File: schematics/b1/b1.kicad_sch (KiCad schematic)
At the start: 0 parts

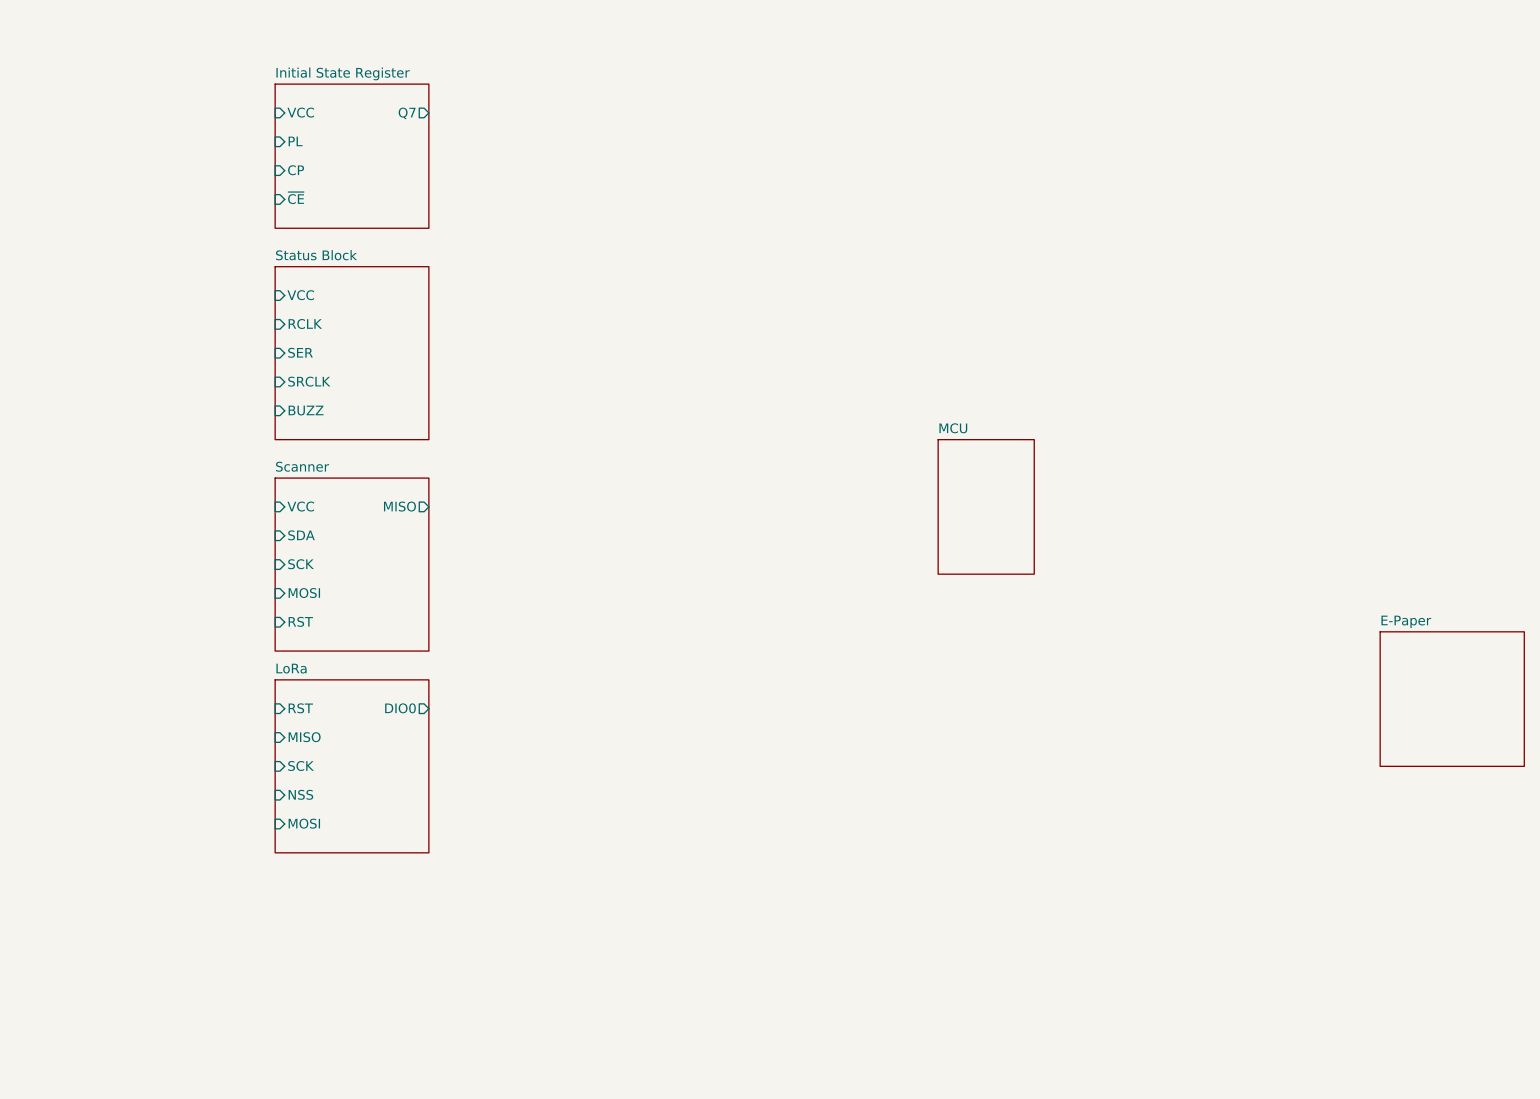
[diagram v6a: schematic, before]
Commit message: Added schematic page for e-paper block.
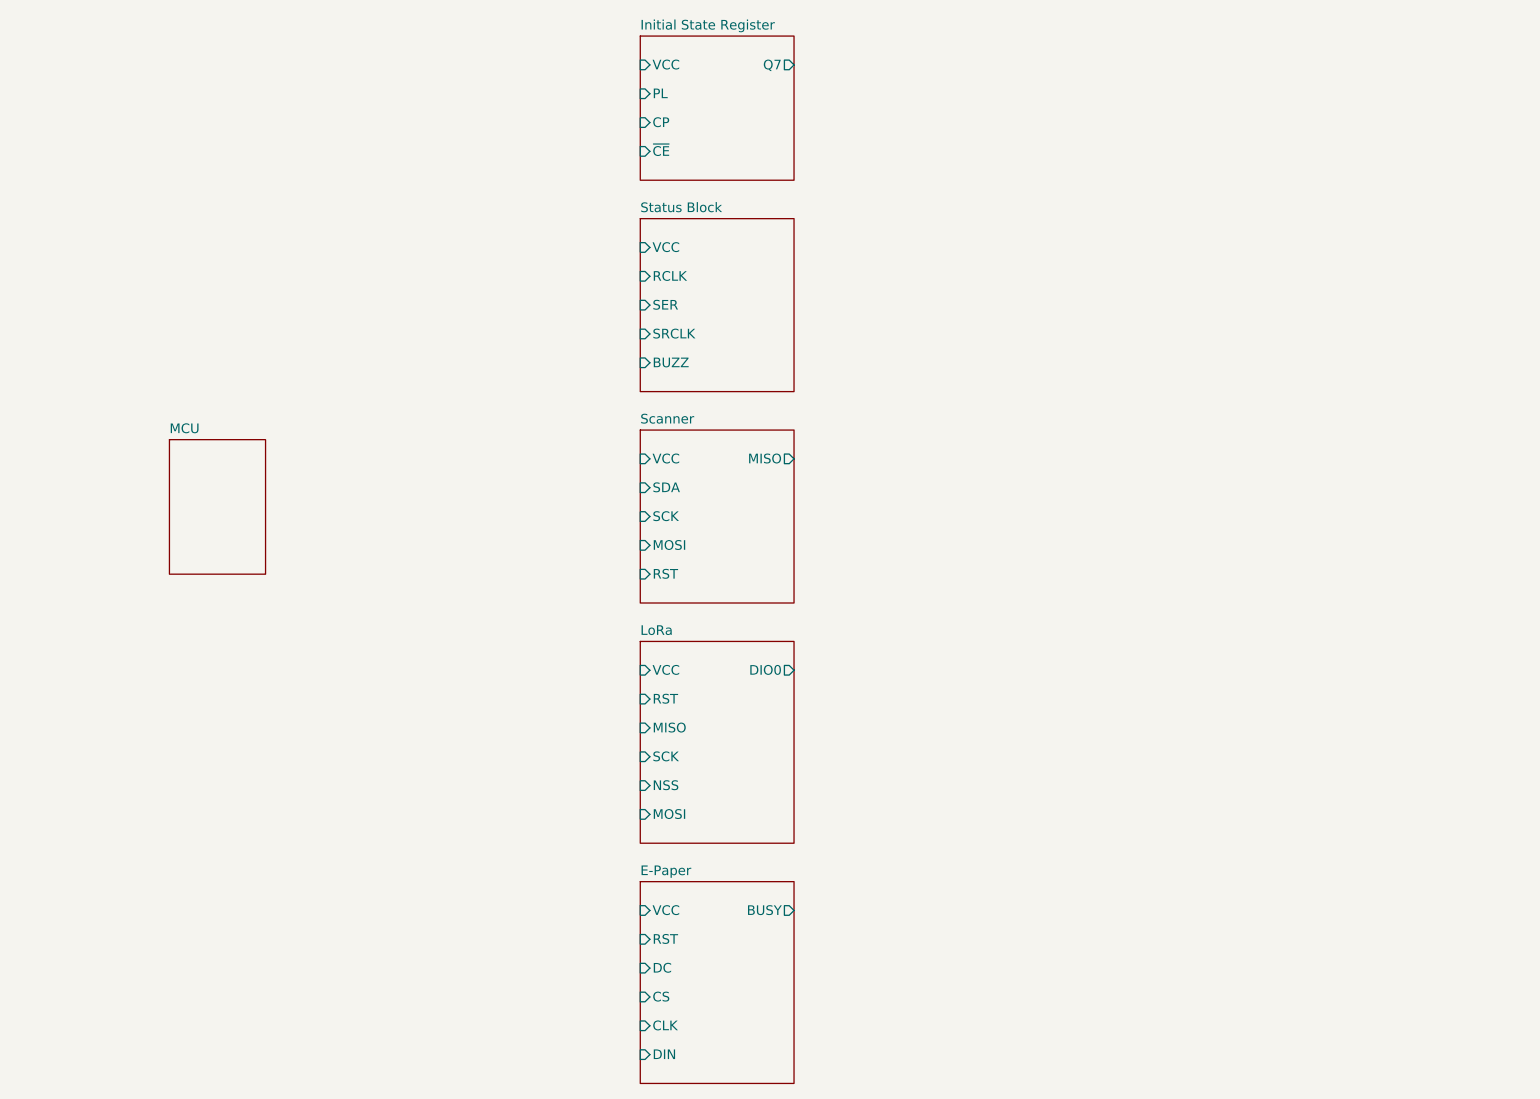
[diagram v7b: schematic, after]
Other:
- sheet E-Paper ports: added BUSY, CLK, CS, DC, DIN, RST, VCC; removed none
- sheet LoRa ports: added VCC; removed none
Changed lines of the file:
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@@
     (comment 4 "A B1 (Badger One) node is the core hardware unit of the Badger sytem. It handles card")
   )
-  (sheet (at 78.74 29.21) (size 20.32 19.05) (fields_autoplaced)
+  (sheet (at 127 22.86) (size 20.32 19.05) (fields_autoplaced)
     (stroke (width 0.1524) (type solid))
     (fill (color 0 0 0 0.0000))
-    (property "Sheetname" "Initial State Register" (at 78.74 28.4984 0)
+    (property "Sheetname" "Initial State Register" (at 127 22.1484 0)
       (effects (font (size 1.27 1.27)) (justify left bottom))
     )
-    (property "Sheetfile" "initial_state_register.kicad_sch" (at 78.74 48.8446 0)
+    (property "Sheetfile" "initial_state_register.kicad_sch" (at 127 42.4946 0)
       (effects (font (size 1.27 1.27)) (justify left top) hide)
     )
-    (pin "PL" input (at 78.74 36.83 180)
+    (pin "PL" input (at 127 30.48 180)
       (effects (font (size 1.27 1.27)) (justify left))
     )
-    (pin "CP" input (at 78.74 40.64 180)
+    (pin "CP" input (at 127 34.29 180)
       (effects (font (size 1.27 1.27)) (justify left))
     )
-    (pin "~{CE}" input (at 78.74 44.45 180)
+    (pin "~{CE}" input (at 127 38.1 180)
       (effects (font (size 1.27 1.27)) (justify left))
     )
-    (pin "Q7" output (at 99.06 33.02 0)
+    (pin "Q7" output (at 147.32 26.67 0)
       (effects (font (size 1.27 1.27)) (justify right))
     )
-    (pin "VCC" input (at 78.74 33.02 180)
+    (pin "VCC" input (at 127 26.67 180)
       (effects (font (size 1.27 1.27)) (justify left))
     )
@@
     )
   )
-  (sheet (at 78.74 81.28) (size 20.32 22.86) (fields_autoplaced)
+  (sheet (at 127 74.93) (size 20.32 22.86) (fields_autoplaced)
     (stroke (width 0.1524) (type solid))
     (fill (color 0 0 0 0.0000))
-    (property "Sheetname" "Scanner" (at 78.74 80.5684 0)
+    (property "Sheetname" "Scanner" (at 127 74.2184 0)
       (effects (font (size 1.27 1.27)) (justify left bottom))
     )
-    (property "Sheetfile" "scanner.kicad_sch" (at 78.74 104.7246 0)
+    (property "Sheetfile" "scanner.kicad_sch" (at 127 98.3746 0)
       (effects (font (size 1.27 1.27)) (justify left top) hide)
     )
-    (pin "MISO" output (at 99.06 85.09 0)
+    (pin "MISO" output (at 147.32 78.74 0)
       (effects (font (size 1.27 1.27)) (justify right))
     )
-    (pin "VCC" input (at 78.74 85.09 180)
+    (pin "VCC" input (at 127 78.74 180)
       (effects (font (size 1.27 1.27)) (justify left))
     )
-    (pin "SDA" input (at 78.74 88.9 180)
+    (pin "SDA" input (at 127 82.55 180)
       (effects (font (size 1.27 1.27)) (justify left))
     )
-    (pin "SCK" input (at 78.74 92.71 180)
+    (pin "SCK" input (at 127 86.36 180)
       (effects (font (size 1.27 1.27)) (justify left))
     )
-    (pin "MOSI" input (at 78.74 96.52 180)
+    (pin "MOSI" input (at 127 90.17 180)
       (effects (font (size 1.27 1.27)) (justify left))
     )
-    (pin "RST" input (at 78.74 100.33 180)
+    (pin "RST" input (at 127 93.98 180)
       (effects (font (size 1.27 1.27)) (justify left))
     )
@@
     )
   )
-  (sheet (at 224.79 101.6) (size 19.05 17.78) (fields_autoplaced)
+  (sheet (at 127 134.62) (size 20.32 26.67) (fields_autoplaced)
     (stroke (width 0.1524) (type solid))
     (fill (color 0 0 0 0.0000))
-    (property "Sheetname" "E-Paper" (at 224.79 100.8884 0)
+    (property "Sheetname" "E-Paper" (at 127 133.9084 0)
       (effects (font (size 1.27 1.27)) (justify left bottom))
     )
-    (property "Sheetfile" "epaper.kicad_sch" (at 224.79 119.9646 0)
+    (property "Sheetfile" "epaper.kicad_sch" (at 127 161.8746 0)
       (effects (font (size 1.27 1.27)) (justify left top) hide)
+    )
+    (pin "BUSY" output (at 147.32 138.43 0)
+      (effects (font (size 1.27 1.27)) (justify right))
+    )
+    (pin "RST" input (at 127 142.24 180)
+      (effects (font (size 1.27 1.27)) (justify left))
+    )
+    (pin "DC" input (at 127 146.05 180)
+      (effects (font (size 1.27 1.27)) (justify left))
+    )
+    (pin "CS" input (at 127 149.86 180)
+      (effects (font (size 1.27 1.27)) (justify left))
+    )
+    (pin "CLK" input (at 127 153.67 180)
+      (effects (font (size 1.27 1.27)) (justify left))
+    )
+    (pin "DIN" input (at 127 157.48 180)
+      (effects (font (size 1.27 1.27)) (justify left))
+    )
+    (pin "VCC" input (at 127 138.43 180)
+      (effects (font (size 1.27 1.27)) (justify left))
     )
     (instances
@@
     )
   )
-  (sheet (at 166.37 76.2) (size 12.7 17.78) (fields_autoplaced)
+  (sheet (at 64.77 76.2) (size 12.7 17.78) (fields_autoplaced)
     (stroke (width 0.1524) (type solid))
     (fill (color 0 0 0 0.0000))
-    (property "Sheetname" "MCU" (at 166.37 75.4884 0)
+    (property "Sheetname" "MCU" (at 64.77 75.4884 0)
       (effects (font (size 1.27 1.27)) (justify left bottom))
     )
-    (property "Sheetfile" "mcu.kicad_sch" (at 166.37 94.5646 0)
+    (property "Sheetfile" "mcu.kicad_sch" (at 64.77 94.5646 0)
       (effects (font (size 1.27 1.27)) (justify left top) hide)
     )
@@
     )
   )
-  (sheet (at 78.74 107.95) (size 20.32 22.86) (fields_autoplaced)
+  (sheet (at 127 102.87) (size 20.32 26.67) (fields_autoplaced)
     (stroke (width 0.1524) (type solid))
     (fill (color 0 0 0 0.0000))
-    (property "Sheetname" "LoRa" (at 78.74 107.2384 0)
+    (property "Sheetname" "LoRa" (at 127 102.1584 0)
       (effects (font (size 1.27 1.27)) (justify left bottom))
     )
-    (property "Sheetfile" "lora.kicad_sch" (at 78.74 131.3946 0)
+    (property "Sheetfile" "lora.kicad_sch" (at 127 130.1246 0)
       (effects (font (size 1.27 1.27)) (justify left top) hide)
     )
-    (pin "DIO0" output (at 99.06 111.76 0)
+    (pin "DIO0" output (at 147.32 106.68 0)
       (effects (font (size 1.27 1.27)) (justify right))
     )
-    (pin "RST" input (at 78.74 111.76 180)
+    (pin "RST" input (at 127 110.49 180)
       (effects (font (size 1.27 1.27)) (justify left))
     )
-    (pin "MISO" input (at 78.74 115.57 180)
+    (pin "MISO" input (at 127 114.3 180)
       (effects (font (size 1.27 1.27)) (justify left))
     )
-    (pin "SCK" input (at 78.74 119.38 180)
+    (pin "SCK" input (at 127 118.11 180)
       (effects (font (size 1.27 1.27)) (justify left))
     )
-    (pin "NSS" input (at 78.74 123.19 180)
+    (pin "NSS" input (at 127 121.92 180)
       (effects (font (size 1.27 1.27)) (justify left))
     )
-    (pin "MOSI" input (at 78.74 127 180)
+    (pin "MOSI" input (at 127 125.73 180)
+      (effects (font (size 1.27 1.27)) (justify left))
+    )
+    (pin "VCC" input (at 127 106.68 180)
       (effects (font (size 1.27 1.27)) (justify left))
     )
@@
     )
   )
-  (sheet (at 78.74 53.34) (size 20.32 22.86) (fields_autoplaced)
+  (sheet (at 127 46.99) (size 20.32 22.86) (fields_autoplaced)
     (stroke (width 0.1524) (type solid))
     (fill (color 0 0 0 0.0000))
-    (property "Sheetname" "Status Block" (at 78.74 52.6284 0)
+    (property "Sheetname" "Status Block" (at 127 46.2784 0)
       (effects (font (size 1.27 1.27)) (justify left bottom))
     )
-    (property "Sheetfile" "status_block.kicad_sch" (at 78.74 76.7846 0)
+    (property "Sheetfile" "status_block.kicad_sch" (at 127 70.4346 0)
       (effects (font (size 1.27 1.27)) (justify left top) hide)
     )
-    (pin "VCC" input (at 78.74 57.15 180)
+    (pin "VCC" input (at 127 50.8 180)
       (effects (font (size 1.27 1.27)) (justify left))
     )
-    (pin "BUZZ" input (at 78.74 72.39 180)
+    (pin "BUZZ" input (at 127 66.04 180)
       (effects (font (size 1.27 1.27)) (justify left))
     )
-    (pin "RCLK" input (at 78.74 60.96 180)
+    (pin "RCLK" input (at 127 54.61 180)
       (effects (font (size 1.27 1.27)) (justify left))
     )
-    (pin "SER" input (at 78.74 64.77 180)
+    (pin "SER" input (at 127 58.42 180)
       (effects (font (size 1.27 1.27)) (justify left))
     )
-    (pin "SRCLK" input (at 78.74 68.58 180)
+    (pin "SRCLK" input (at 127 62.23 180)
       (effects (font (size 1.27 1.27)) (justify left))
     )

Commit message: Updated labels.
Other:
- sheet E-Paper ports: added ~{CS}, ~{RST}; removed CS, RST
- sheet Initial State Register ports: added ~{PL}; removed PL
- sheet LoRa ports: added ~{NSS}, ~{RESET}; removed NSS, RST
- sheet Scanner ports: added ~{SS}; removed SCK
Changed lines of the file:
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@@
       (effects (font (size 1.27 1.27)) (justify left top) hide)
-    )
-    (pin "PL" input (at 127 30.48 180)
-      (effects (font (size 1.27 1.27)) (justify left))
     )
     (pin "CP" input (at 127 34.29 180)
@@
     )
     (pin "VCC" input (at 127 26.67 180)
+      (effects (font (size 1.27 1.27)) (justify left))
+    )
+    (pin "~{PL}" input (at 127 30.48 180)
       (effects (font (size 1.27 1.27)) (justify left))
     )
@@
       (effects (font (size 1.27 1.27)) (justify left))
     )
-    (pin "SCK" input (at 127 86.36 180)
-      (effects (font (size 1.27 1.27)) (justify left))
-    )
     (pin "MOSI" input (at 127 90.17 180)
       (effects (font (size 1.27 1.27)) (justify left))
     )
     (pin "RST" input (at 127 93.98 180)
+      (effects (font (size 1.27 1.27)) (justify left))
+    )
+    (pin "~{SS}" input (at 127 86.36 180)
       (effects (font (size 1.27 1.27)) (justify left))
     )
@@
       (effects (font (size 1.27 1.27)) (justify right))
     )
-    (pin "RST" input (at 127 142.24 180)
-      (effects (font (size 1.27 1.27)) (justify left))
-    )
     (pin "DC" input (at 127 146.05 180)
-      (effects (font (size 1.27 1.27)) (justify left))
-    )
-    (pin "CS" input (at 127 149.86 180)
       (effects (font (size 1.27 1.27)) (justify left))
     )
@@
     )
     (pin "VCC" input (at 127 138.43 180)
+      (effects (font (size 1.27 1.27)) (justify left))
+    )
+    (pin "~{RST}" input (at 127 142.24 180)
+      (effects (font (size 1.27 1.27)) (justify left))
+    )
+    (pin "~{CS}" input (at 127 149.86 180)
       (effects (font (size 1.27 1.27)) (justify left))
     )
@@
       (effects (font (size 1.27 1.27)) (justify right))
     )
-    (pin "RST" input (at 127 110.49 180)
-      (effects (font (size 1.27 1.27)) (justify left))
-    )
     (pin "MISO" input (at 127 114.3 180)
       (effects (font (size 1.27 1.27)) (justify left))
@@
       (effects (font (size 1.27 1.27)) (justify left))
     )
-    (pin "NSS" input (at 127 121.92 180)
-      (effects (font (size 1.27 1.27)) (justify left))
-    )
     (pin "MOSI" input (at 127 125.73 180)
       (effects (font (size 1.27 1.27)) (justify left))
     )
     (pin "VCC" input (at 127 106.68 180)
+      (effects (font (size 1.27 1.27)) (justify left))
+    )
+    (pin "~{NSS}" input (at 127 121.92 180)
+      (effects (font (size 1.27 1.27)) (justify left))
+    )
+    (pin "~{RESET}" input (at 127 110.49 180)
       (effects (font (size 1.27 1.27)) (justify left))
     )
@@
       (effects (font (size 1.27 1.27)) (justify left))
     )
-    (pin "RCLK" input (at 127 54.61 180)
-      (effects (font (size 1.27 1.27)) (justify left))
-    )
     (pin "SER" input (at 127 58.42 180)
       (effects (font (size 1.27 1.27)) (justify left))
@@
       (effects (font (size 1.27 1.27)) (justify left))
     )
+    (pin "RCLK" input (at 127 54.61 180)
+      (effects (font (size 1.27 1.27)) (justify left))
+    )
